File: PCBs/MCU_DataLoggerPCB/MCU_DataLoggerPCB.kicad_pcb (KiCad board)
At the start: 2 copper layers, 53.8 x 36.1 mm, 29 parts, among them J1 Conn_01x04_Pin, J2 Conn_01x04_Pin, J3 Conn_01x09_Pin, J4 Conn_02x03_Odd_Even, U1 24LC1025, U2 24LC1025, U3 DS1337S+, U4 ATMEGA328P-AU, Y1 32.768 kHz, Y2 16 MHz

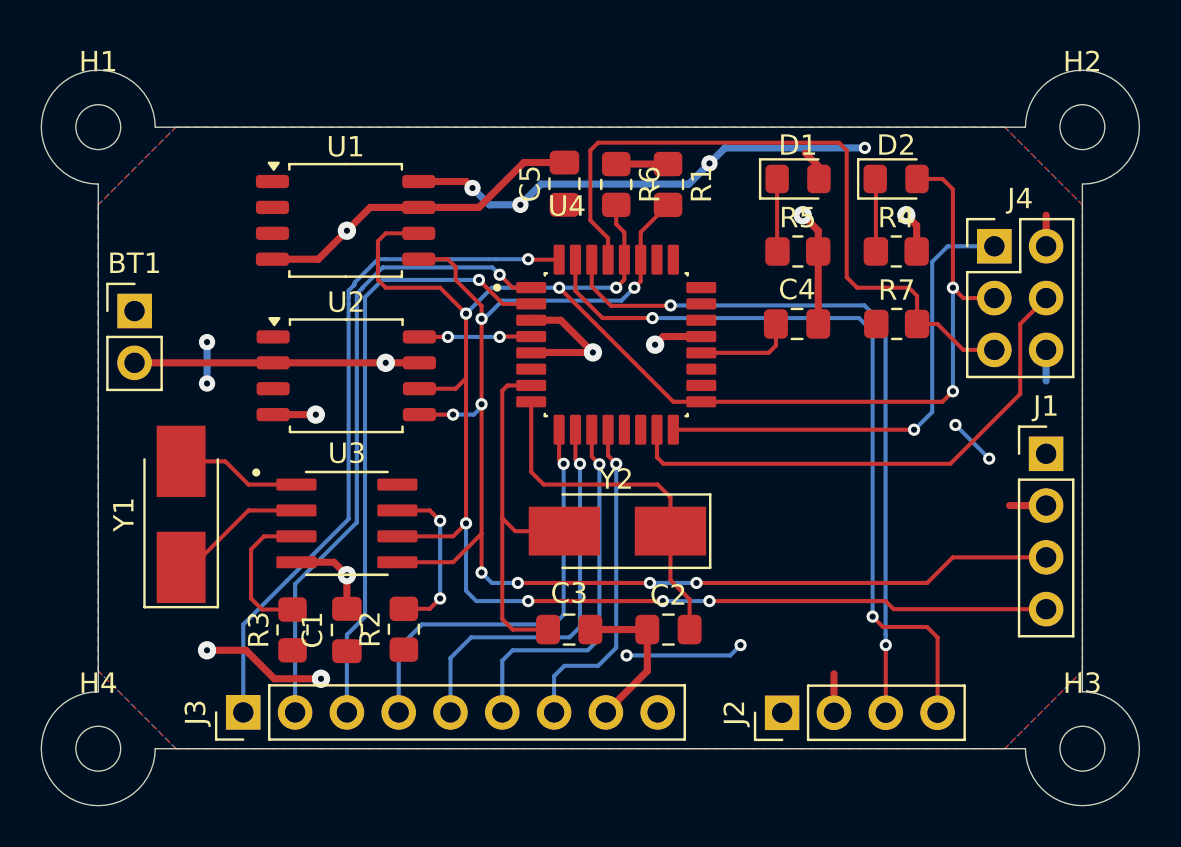
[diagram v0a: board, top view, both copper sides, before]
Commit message: Project: Completed putting silkscreen on the PCB
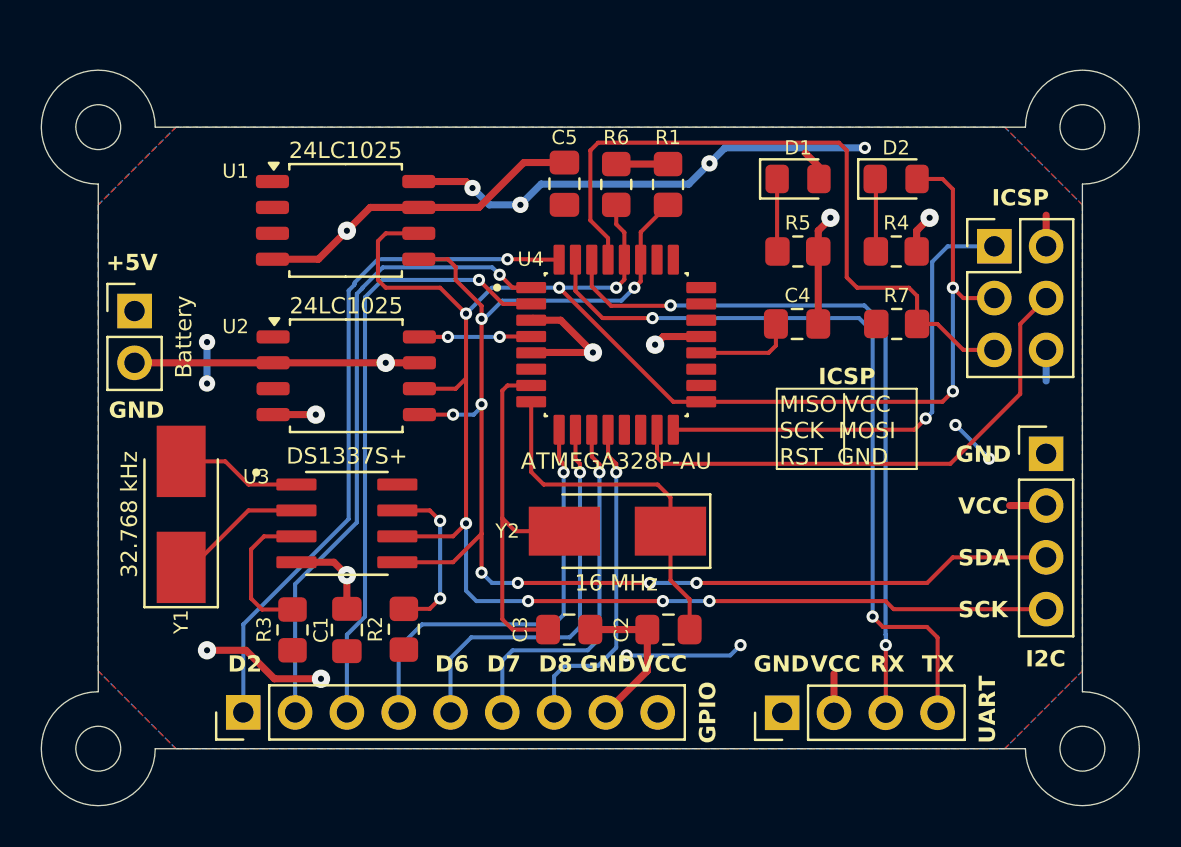
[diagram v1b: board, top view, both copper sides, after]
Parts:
- added REF**: KiCad-Logo2_5mm_SilkScreen, Symbol:KiCad-Logo2_5mm_SilkScreen, B.Cu at (69.8, 75.8)
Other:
- board text added: "+5V"
- board text added: "- 2Mbit EEPROM - RTC - I2C, SPI, GPIOs"
- board text added: "D2"
- board text added: "D6"
- board text added: "D7"
- board text added: "D8"
- board text added: "Data Logger with the ATMega328P"
- board text added: "GND"
- board text added: "GPIO"
- board text added: "I2C"
- board text added: "ICSP"
- board text added: "KT"
- board text added: "MISO VCC SCK MOSI RST GND"
- board text added: "RX"
- board text added: "SCK"
- board text added: "SDA"
- board text added: "TX"
- board text added: "UART"
- board text added: "VCC"

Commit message: Project: Fixed the same error but on PCB
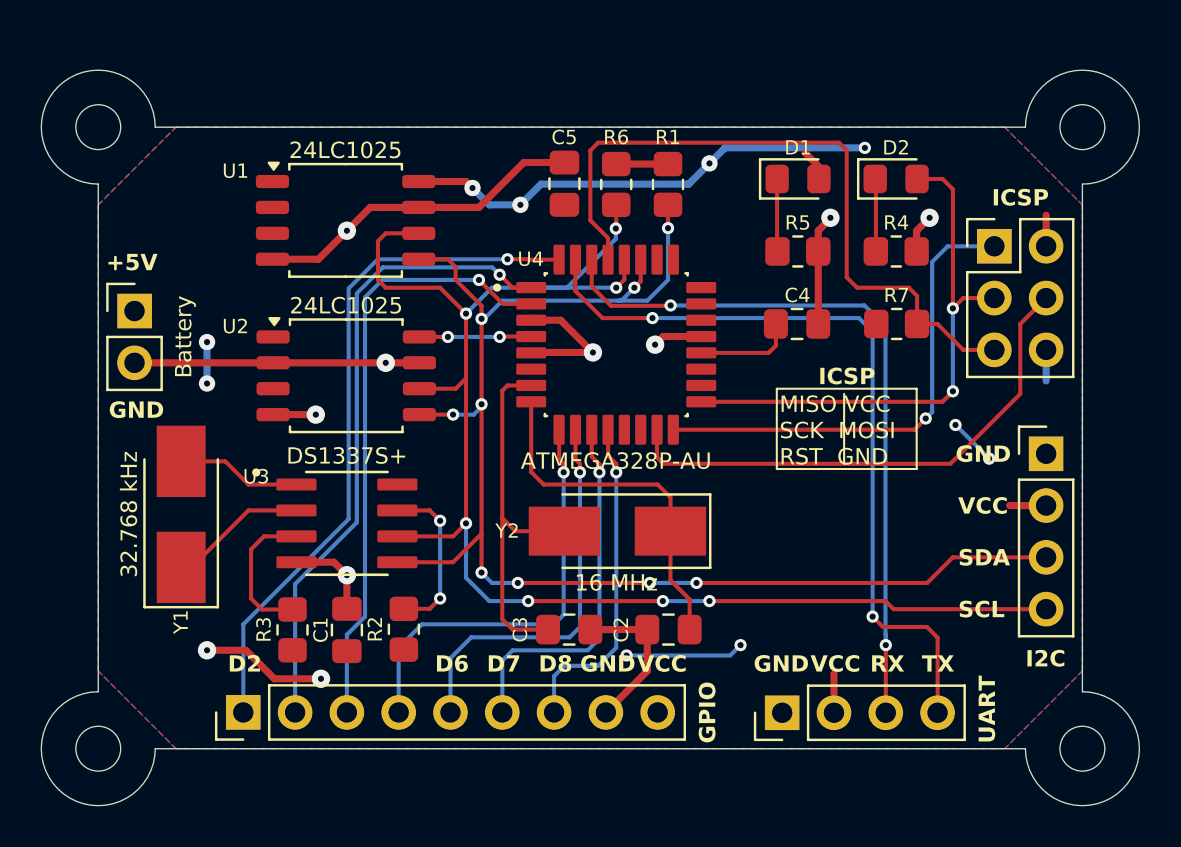
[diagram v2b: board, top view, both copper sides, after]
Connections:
- J1 pad 4: /SCK -> /SCL
- R6 pad 2: /SCK -> /SCL
- U1 pad 6: /SCK -> /SCL
- U2 pad 6: /SCK -> /SCL
- U3 pad 6: /SCK -> /SCL
- U4 pad 28: /SCK -> /SCL
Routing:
- net /SCK: track 105.8 -> 26.7 mm, vias 9 -> 2
- net /SCL: track 0.00 -> 73.1 mm, vias 0 -> 7
- net /SDA: track 66.8 -> 70.1 mm, vias 8 -> 9
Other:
- board text added: "SCL"
- board text removed: "SCK"
